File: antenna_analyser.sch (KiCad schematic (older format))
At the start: 29 parts, among them IC1 MCP6002, IC2 ARDUINO_PRO_MINI_5V, P1 AD9850_CONN, U1 AMS1117

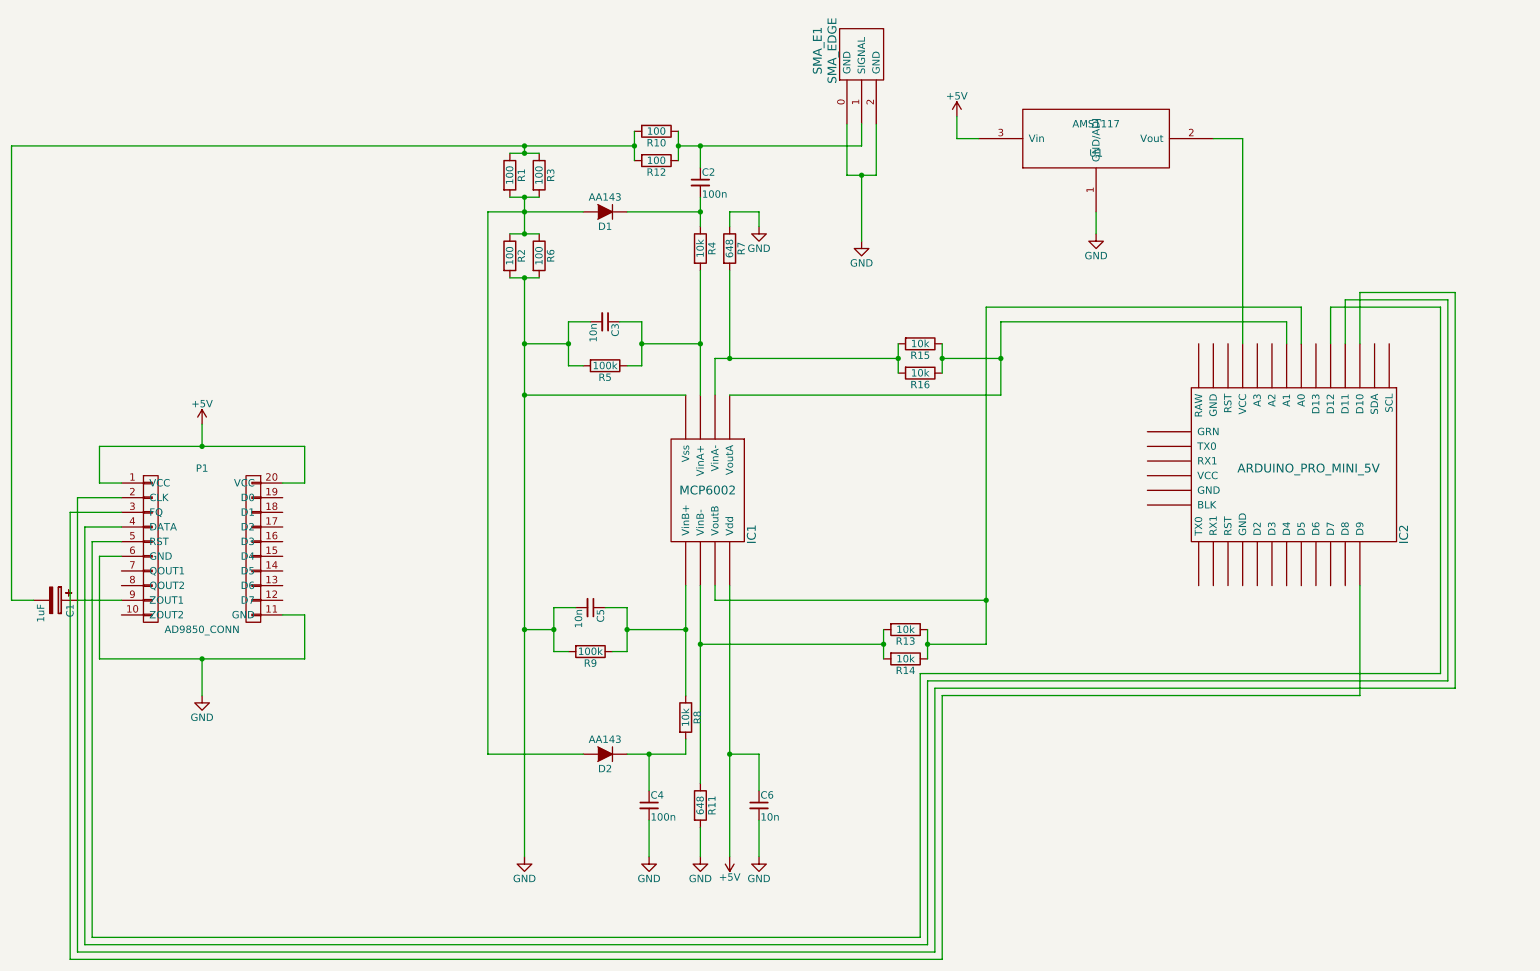
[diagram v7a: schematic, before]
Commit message: Added a connector for the LCD display.
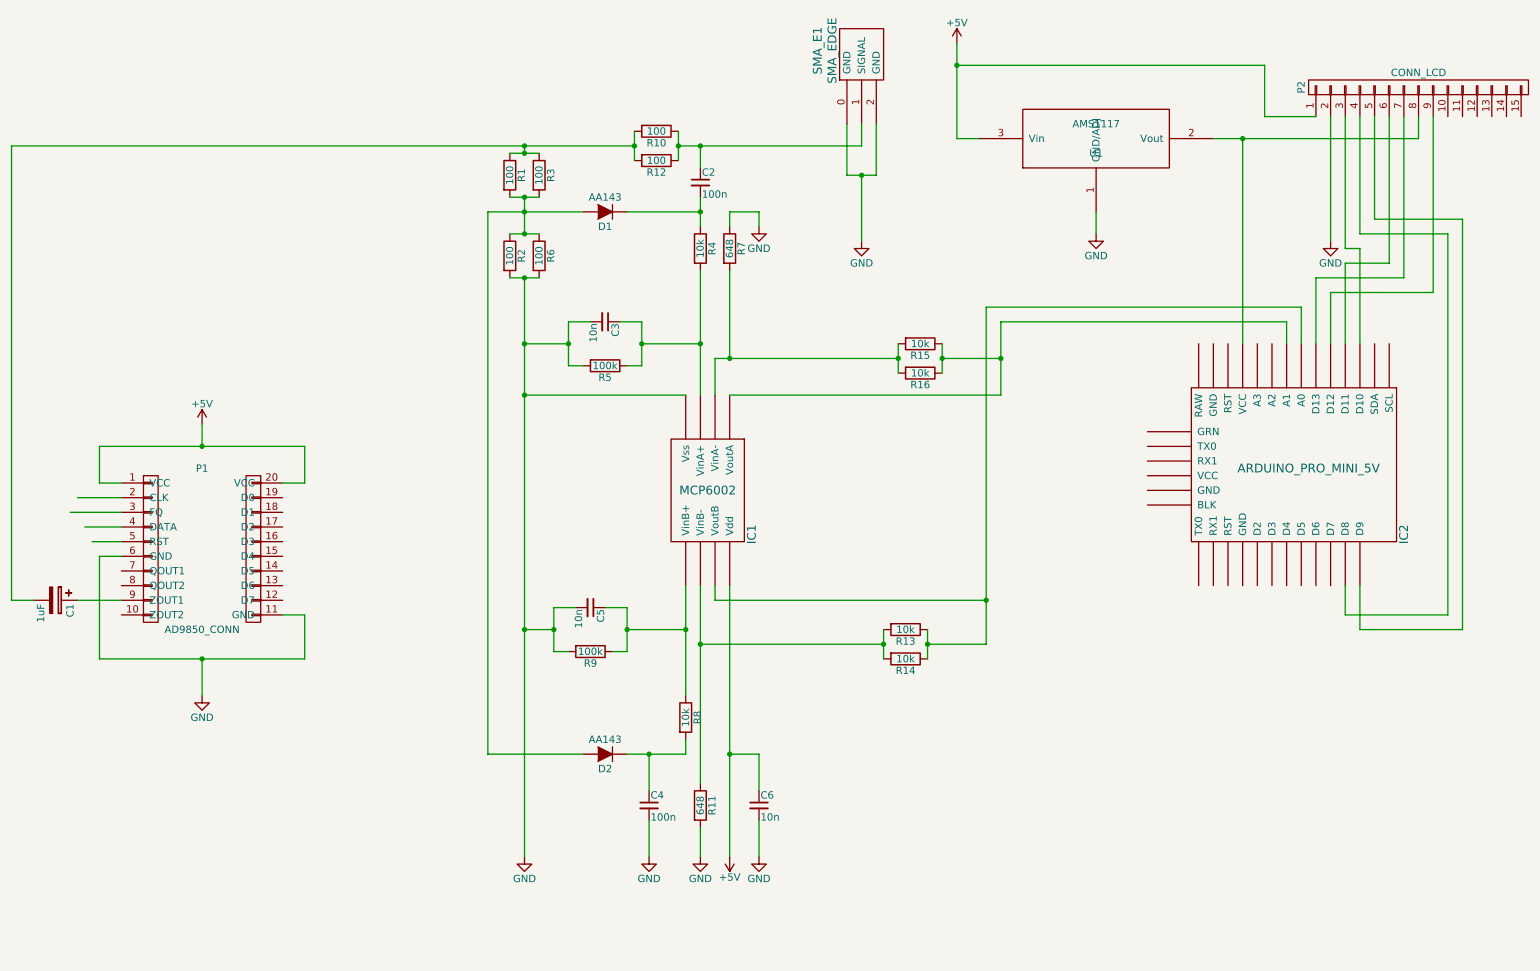
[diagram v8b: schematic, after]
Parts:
- added P2: CONN_LCD, symbol CONN_01X15
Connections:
- wire segments 123 -> 124
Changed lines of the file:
@@
 	8950 2750 8950 1350
 Wire Wire Line
-	8950 1350 8750 1350
+	8750 1350 10150 1350
 Wire Wire Line
 	7950 1850 7950 2000
@@
 L +5V #PWR07
 U 1 1 558DD6BD
-P 7000 1200
-F 0 "#PWR07" H 7000 1050 50  0001 C CNN
-F 1 "+5V" H 7000 1340 50  0000 C CNN
-F 2 "" H 7000 1200 60  0000 C CNN
-F 3 "" H 7000 1200 60  0000 C CNN
-	1    7000 1200
+P 7000 700
+F 0 "#PWR07" H 7000 550 50  0001 C CNN
+F 1 "+5V" H 7000 840 50  0000 C CNN
+F 2 "" H 7000 700 60  0000 C CNN
+F 3 "" H 7000 700 60  0000 C CNN
+	1    7000 700
 	1    0    0    -1
 $EndComp
@@
 	7150 1350 7000 1350
 Wire Wire Line
-	7000 1350 7000 1200
+	7000 1350 7000 700
 $Comp
 L GND #PWR08
@@
 	1300 4100 1100 4100
 Wire Wire Line
-	1100 4100 1100 6800
-Wire Wire Line
-	1100 6800 6750 6800
-Wire Wire Line
-	6750 6800 6750 5000
-Wire Wire Line
-	6750 5000 10300 5000
-Wire Wire Line
-	9550 2750 9550 2500
-Wire Wire Line
-	9550 2500 10300 2500
-Wire Wire Line
-	10300 2500 10300 5000
-Wire Wire Line
 	1300 4000 1050 4000
 Wire Wire Line
-	1050 4000 1050 6850
-Wire Wire Line
-	1050 6850 6800 6850
-Wire Wire Line
-	6800 6850 6800 5050
-Wire Wire Line
-	6800 5050 10350 5050
-Wire Wire Line
-	10350 5050 10350 2450
-Wire Wire Line
-	10350 2450 9650 2450
-Wire Wire Line
-	9650 2450 9650 2750
-Wire Wire Line
 	1300 3800 1000 3800
 Wire Wire Line
-	1000 3800 1000 6900
-Wire Wire Line
-	1000 6900 6850 6900
-Wire Wire Line
-	6850 6900 6850 5100
-Wire Wire Line
-	6850 5100 10400 5100
-Wire Wire Line
-	10400 5100 10400 2400
-Wire Wire Line
-	10400 2400 9750 2400
-Wire Wire Line
-	9750 2400 9750 2750
-Wire Wire Line
 	1300 3900 950  3900
-Wire Wire Line
-	950  3900 950  6950
-Wire Wire Line
-	950  6950 6900 6950
-Wire Wire Line
-	6900 6950 6900 5150
-Wire Wire Line
-	6900 5150 9750 5150
-Wire Wire Line
-	9750 5150 9750 4400
 $Comp
 L R R2
@@
 	5150 3100 4050 3100
 Connection ~ 4050 3100
+$Comp
+L CONN_01X15 P2
+U 1 1 55904C18
+P 10150 1000
+F 0 "P2" H 10150 1800 50  0000 C CNN
+F 1 "CONN_LCD" V 10250 1000 50  0000 C CNN
+F 2 "" H 10150 1000 60  0000 C CNN
+F 3 "" H 10150 1000 60  0000 C CNN
+	1    10150 1000
+	0    -1   -1   0
+$EndComp
+Wire Wire Line
+	9450 1200 9100 1200
+Wire Wire Line
+	9100 1200 9100 850
+Wire Wire Line
+	9100 850  7000 850
+Connection ~ 7000 850
+$Comp
+L GND #PWR?
+U 1 1 55904F2C
+P 9550 2050
+F 0 "#PWR?" H 9550 1800 50  0001 C CNN
+F 1 "GND" H 9550 1900 50  0000 C CNN
+F 2 "" H 9550 2050 60  0000 C CNN
+F 3 "" H 9550 2050 60  0000 C CNN
+	1    9550 2050
+	1    0    0    -1
+$EndComp
+Wire Wire Line
+	9550 2050 9550 1200
+Wire Wire Line
+	9750 1200 9750 2000
+Wire Wire Line
+	9750 2000 10350 2000
+Wire Wire Line
+	10350 2000 10350 4600
+Wire Wire Line
+	10350 4600 9650 4600
+Wire Wire Line
+	9650 4600 9650 4400
+Wire Wire Line
+	9850 1200 9850 1900
+Wire Wire Line
+	9850 1900 10450 1900
+Wire Wire Line
+	10450 1900 10450 4700
+Wire Wire Line
+	10450 4700 9750 4700
+Wire Wire Line
+	9750 4700 9750 4400
+Wire Wire Line
+	9650 1200 9650 2100
+Wire Wire Line
+	9650 2100 9750 2100
+Wire Wire Line
+	9750 2100 9750 2750
+Wire Wire Line
+	9950 1200 9950 2200
+Wire Wire Line
+	9950 2200 9650 2200
+Wire Wire Line
+	9650 2200 9650 2750
+Wire Wire Line
+	10050 1200 10050 2300
+Wire Wire Line
+	10050 2300 9450 2300
+Wire Wire Line
+	9450 2300 9450 2750
+Wire Wire Line
+	10150 1350 10150 1200
+Connection ~ 8950 1350
+Wire Wire Line
+	10250 1200 10250 2400
+Wire Wire Line
+	10250 2400 9550 2400
+Wire Wire Line
+	9550 2400 9550 2750
 $EndSCHEMATC
